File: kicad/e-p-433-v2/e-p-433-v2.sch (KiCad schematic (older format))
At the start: 35 parts, among them J1 2 X thermomètre digital, P1 ant, P2 Transmitter, SW1 SW_SPDT, SW2 SW_DIP_x01, SW3 SW_DIP_x01, U1 PRT-10401, U2 Teensy_3-2, Y1 Cristal, 32.768 kHz

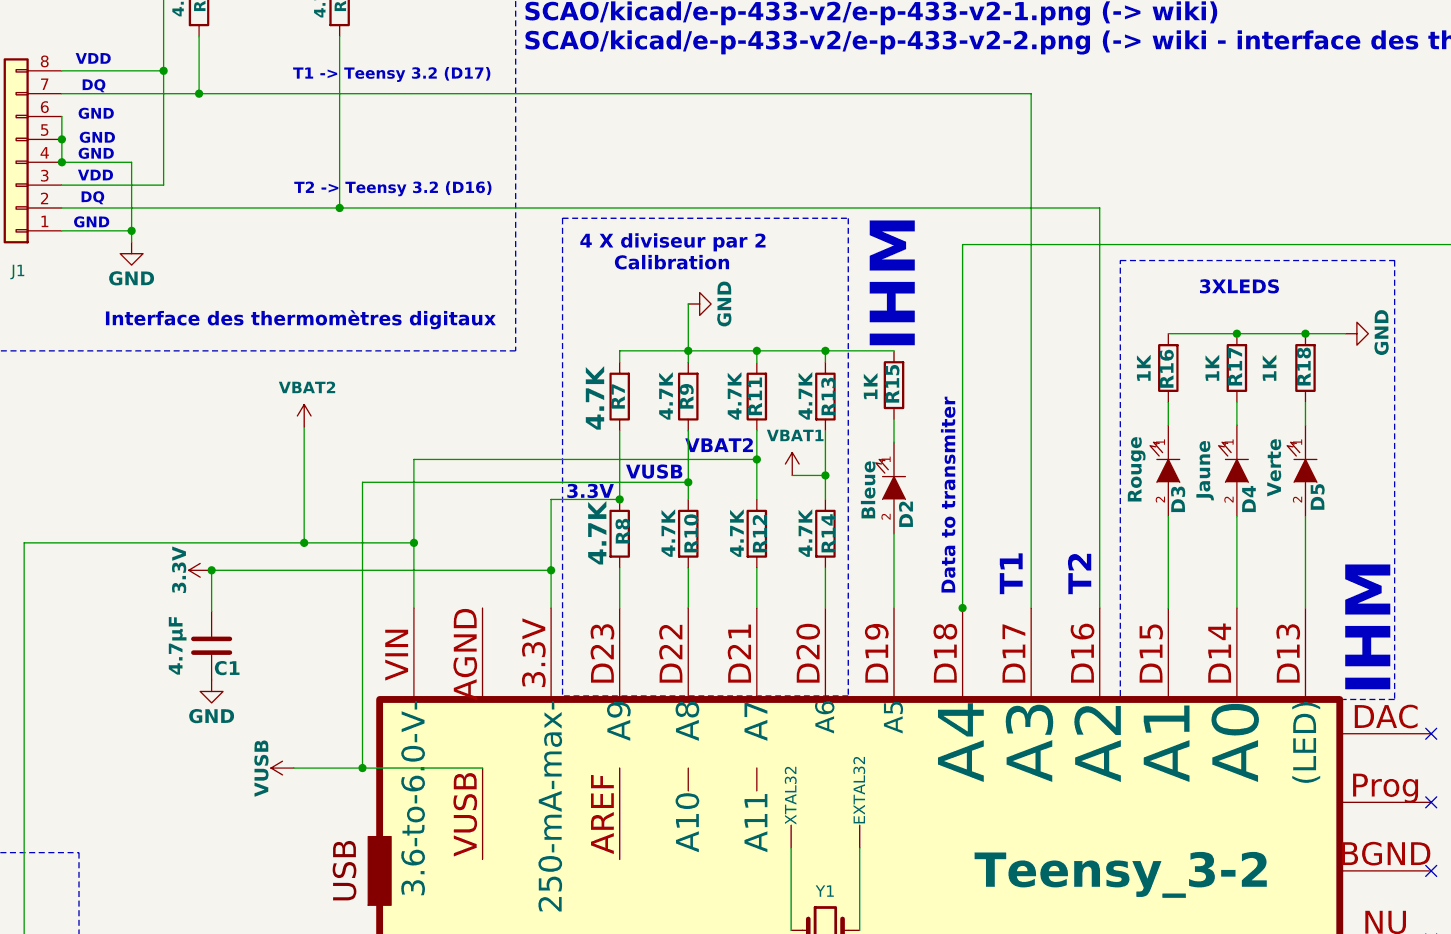
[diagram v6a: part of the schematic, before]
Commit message: Correction erreur sur pont diviseur
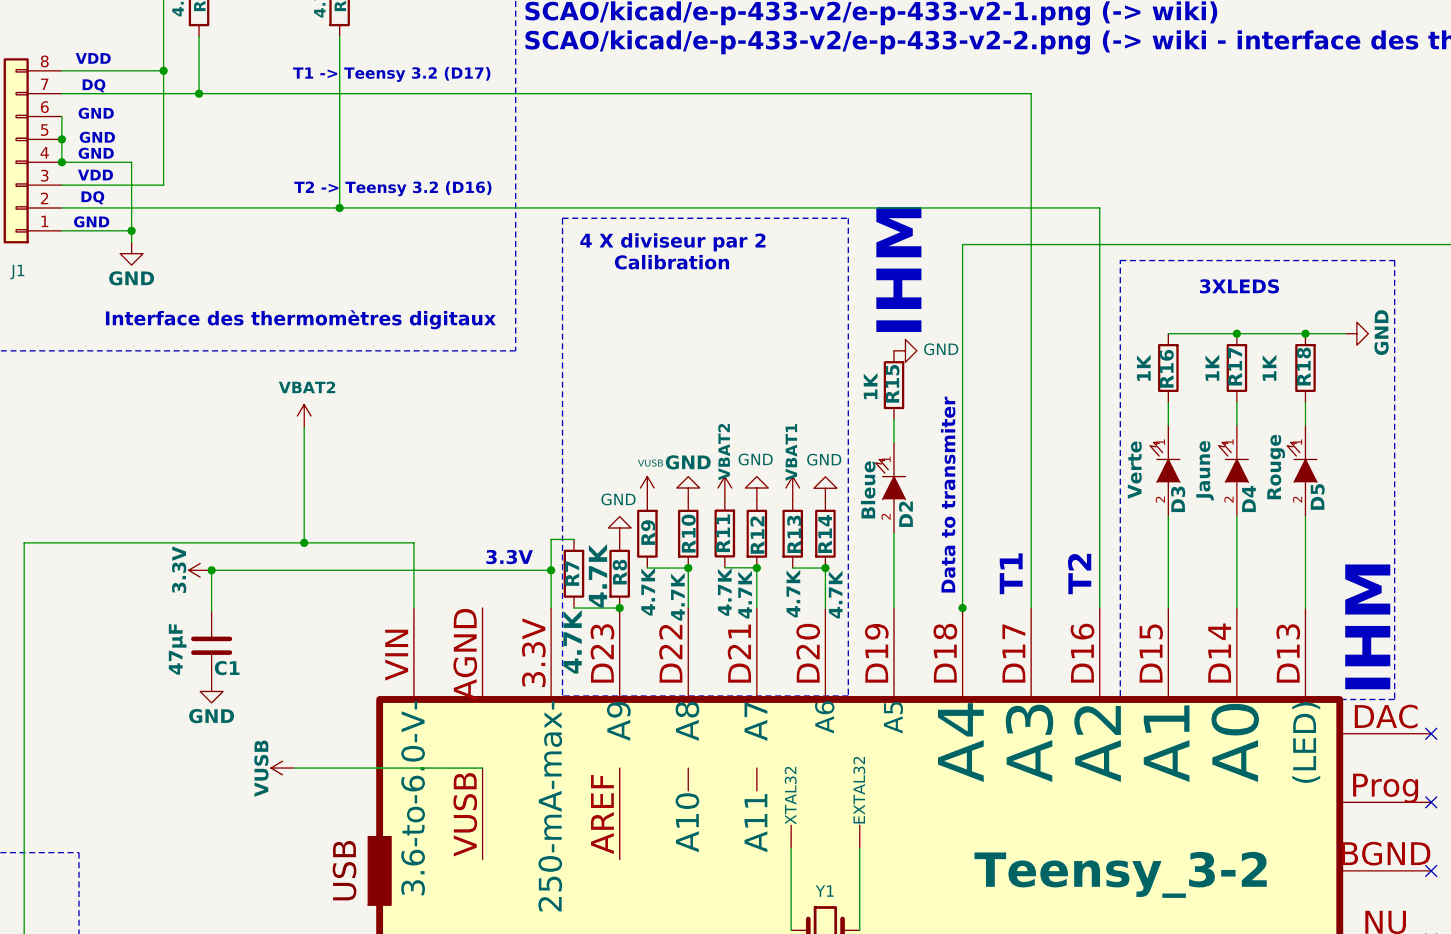
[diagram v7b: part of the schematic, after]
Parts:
- C1: value 4.7µF -> 47µF
- D3: value Rouge -> Verte
- D5: value Verte -> Rouge
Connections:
- net +5V: now also R9.2; no longer R10.1, R9.1
- net +BATT: now also R11.2, R13.1; no longer R11.1, R12.1, R13.2, R14.1
- net 3.3V: now also R7.2; no longer R7.1, R8.1
- net GND: now also R10.1, R12.1, R14.1, R8.1; no longer R11.2, R13.1, R7.2, R9.2
- net at R12.2, U2.D21 (A7): now also R11.1
- net at R10.2, U2.D22 (A8): now also R9.1
- net at R8.2, U2.D23 (A9): now also R7.1
- net at R14.2, U2.D20 (A6): now also R13.2
- net at U2.~ (XTAL32): now also Y1.2
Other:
- note removed: "VUSB"
- moved on the sheet: R11, R13, R7, R8, R9
